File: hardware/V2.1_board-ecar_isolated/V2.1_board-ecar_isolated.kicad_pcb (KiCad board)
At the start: 4 copper layers, 160 x 100 mm, 116 parts, among them IC1 ATMEGA8A-P, J1 2x BATT IN, J10 24V, J11 18V, J12 5V, J13 ADC reserve [5V, in, GND], J14 IGBT [Gate, GND], J16 UART [TX, RX, GND], J17 2x Switch (to 5V) [PC3, PC2], J18 Relay contacts [NO, COM, NC], J19 [5V, 5V-decoupled], J2 ST 2x GND power, J21 ADC reserve, J23 2x 24V filtered, J24 Fan [GND/Mosfet-OUT, Diode, 2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, J4 2x GND (5V), J5 PWM-Signal, J6 LED 3,2V 20mA [-, +], J7 Gas Pedal [5V, In, GND], J8 Gate, J9 BATT-F, K1 24V relay, P1 ISP, Q1 BC547, Q2 IRFZ24N, U1 LM7818CT, U3 TC429, U4 LM358N

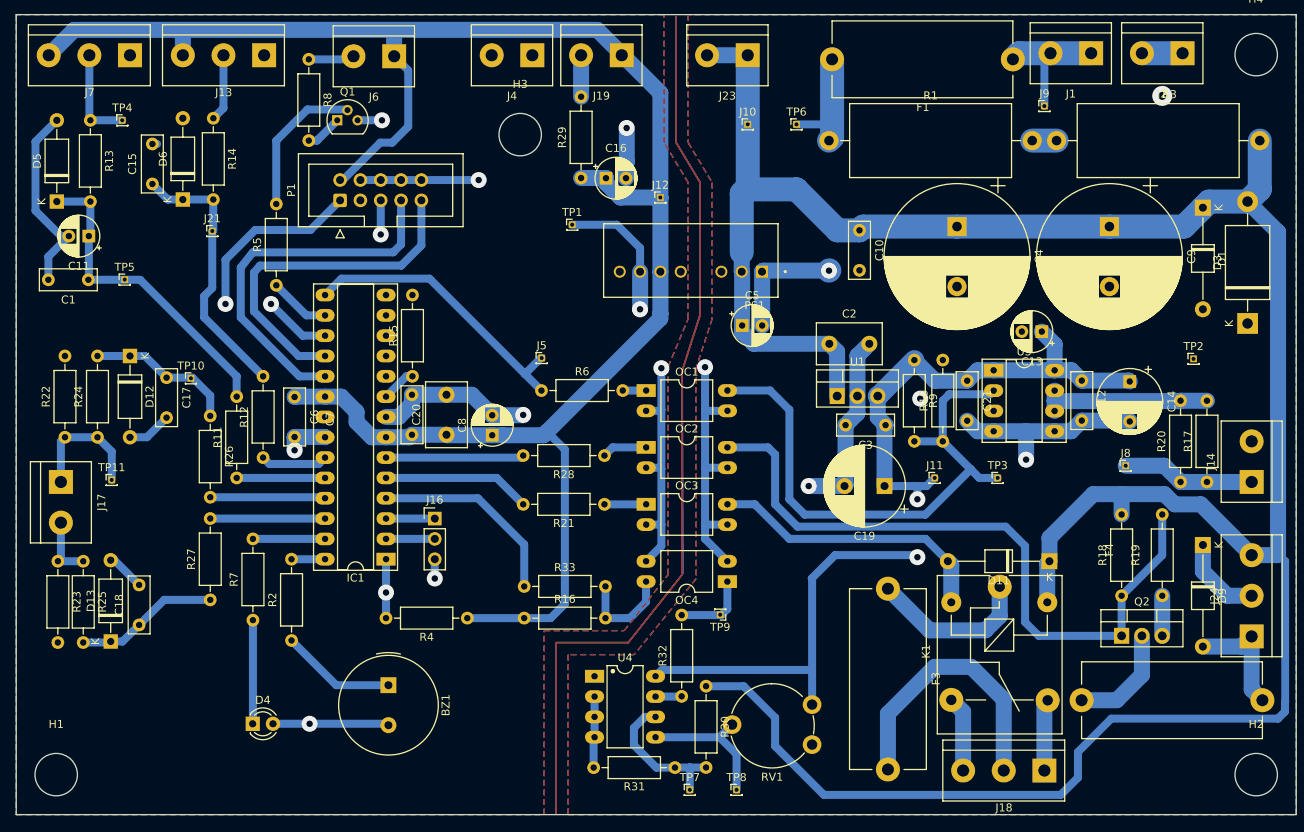
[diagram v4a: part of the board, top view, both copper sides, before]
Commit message: pcb: optimize silk, change values
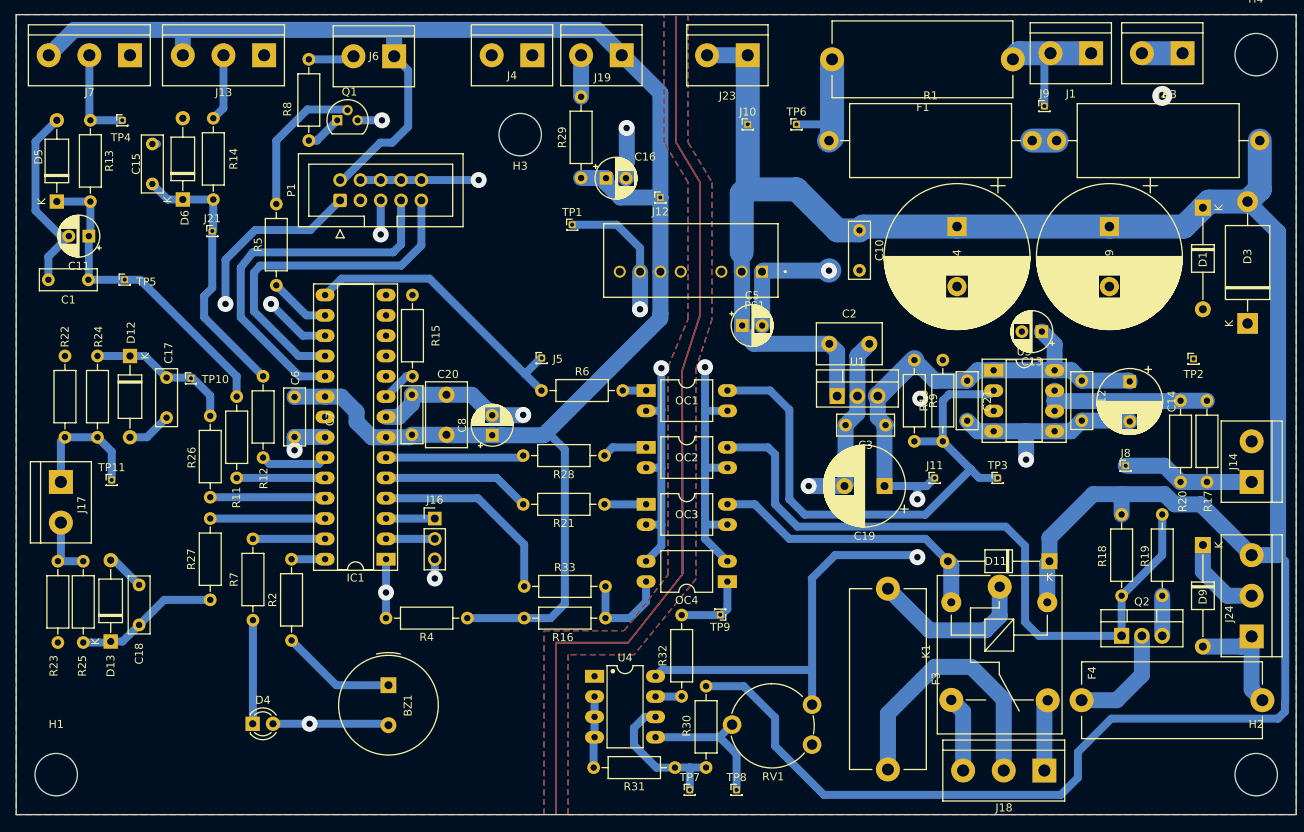
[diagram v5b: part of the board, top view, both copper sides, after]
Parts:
- J16: value UART [TX, RX, GND] -> UART [GND, RX, TX]
- R21, R28: value 200 -> 510
- R32: value 1k -> 2k4

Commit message: V2.1 pcb finished, exports, photos, readme
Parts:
- R17: value 0 -> 10
- R9: value 12k (15k used) -> 15k
- TP3: value DRV-in -> Driver-in
- TP4: value GP-in -> Pedal-in
- TP5: value GP-filtered -> Pedal-filtered
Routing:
- net GNDPWR: vias 6 -> 5
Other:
- board text added: "PCB Supply BATT, BATT GND, GND"
- board text removed: "(5mm LED 3,2V 20mA) (Pin-28/PC5) - +"
- board text removed: "20-35V with peaks"
- board text removed: "24V 24V"
- board text removed: "5V 5V"
- board text removed: "GND GND"
- board text removed: "NO, COM, NC Relay (Pin-10/PB7)"
- board text removed: "PCB Supply: BATT, BATT"
- board text removed: "PCB Supply: GND GND"
